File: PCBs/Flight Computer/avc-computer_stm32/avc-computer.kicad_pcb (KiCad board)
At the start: 2 copper layers, 57.8 x 87.2 mm, 54 parts, among them IC1 MP2307, J1 Conn_ARM_JTAG_SWD_10, J2 Conn_01x02_Female, J3 ESP_01_Socket, J4 ESC Power, J5 ESC Connector, J6 OLED Display, U1 CAT24M01W, U2 CAT24M01W, U3 STM32F103C8Tx, U4 BNO085, U5 CAT24M01W, U6 CAT24M01W, U7 LD1117S33TR_SOT223, U8 BMP581

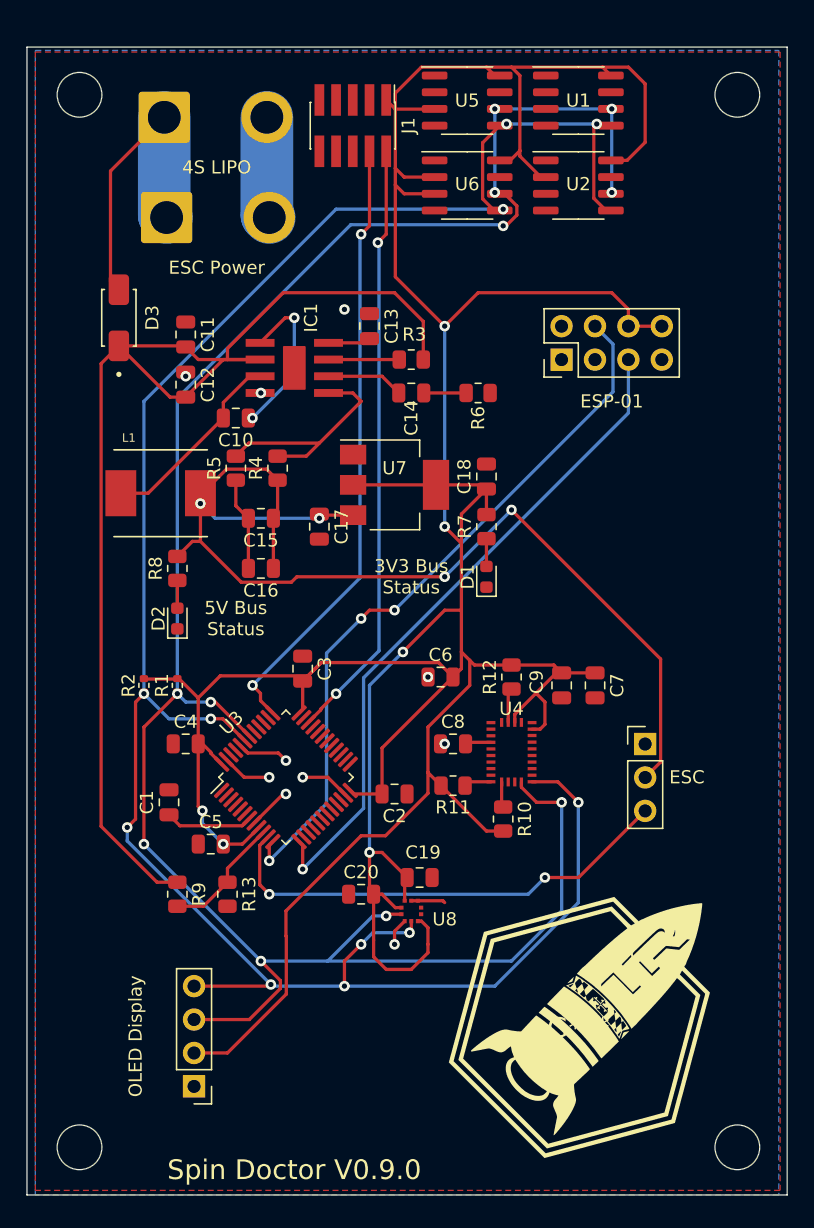
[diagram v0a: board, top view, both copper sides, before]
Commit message: Renamed folder
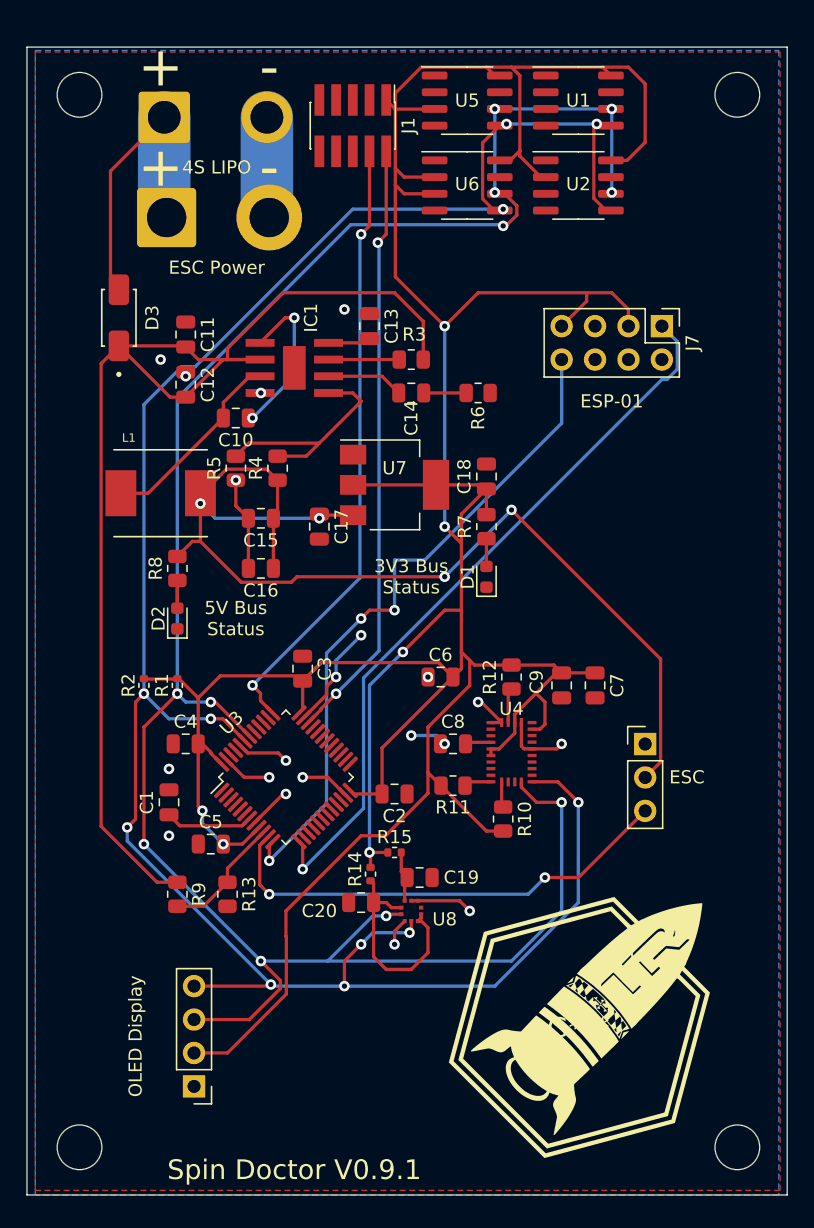
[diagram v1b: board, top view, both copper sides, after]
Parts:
- removed J3: ESP_01_Socket, Connector_PinHeader_2.54mm:PinHeader_2x04_P2.54mm_Vertical
- added J7: Conn_02x04_Odd_Even, Connector_PinHeader_2.54mm:PinHeader_2x04_P2.54mm_Vertical, F.Cu at (141.6, 76.8)
- added R14: 10, Resistor_SMD:R_0402_1005Metric, F.Cu at (119.5, 118.5)
- added R15: 10, Resistor_SMD:R_0402_1005Metric, F.Cu at (121.3, 116.8)
- R13: value 198 -> 200
- moved C20 0.64 mm to (118.7, 120.7)
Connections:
- C19 pad 2: +3V3 -> Net-(U8-VDD)
- C20 pad 2: +3V3 -> Net-(U8-CSB)
- U8 pad 1: +3V3 -> Net-(U8-CSB)
- U8 pad 10: +3V3 -> Net-(U8-VDD)
- U8 pad 5: +3V3 -> Net-(U8-CSB)
- U8 pad 6: unconnected-(U8-Pad6) -> Net-(U8-CSB)
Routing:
- net GND: track 34.4 -> 55.8 mm, vias 10 -> 20
- net +3V3: track 312.0 -> 295.0 mm
- net Net-(U8-CSB): track 0.00 -> 16.7 mm
- net /Microcontroller/PA3: track 51.2 -> 56.0 mm
- net Net-(U8-VDD): track 0.00 -> 3.93 mm
- net /Microcontroller/PA2: track 54.7 -> 51.3 mm
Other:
- board text added: "+"
- board text added: "-"
- board text added: "Spin Doctor V0.9.1"
- board text removed: "Spin Doctor V0.9.0"

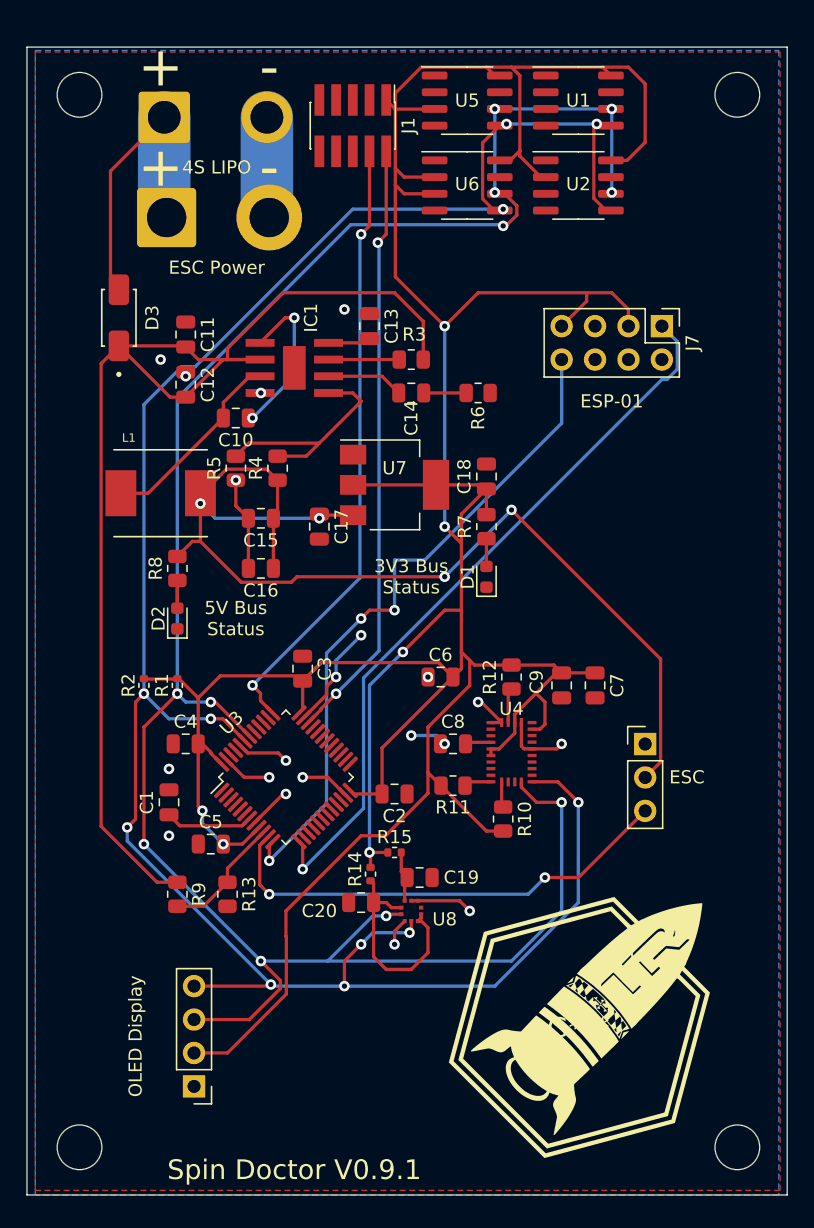
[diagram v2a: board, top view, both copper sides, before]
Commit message: Relpaced swithcing regulator with linear regulator. Removed unneccesary components. Replaced barometric pressure sensor with better one. Added connectors for brake servo & hall effect sensor
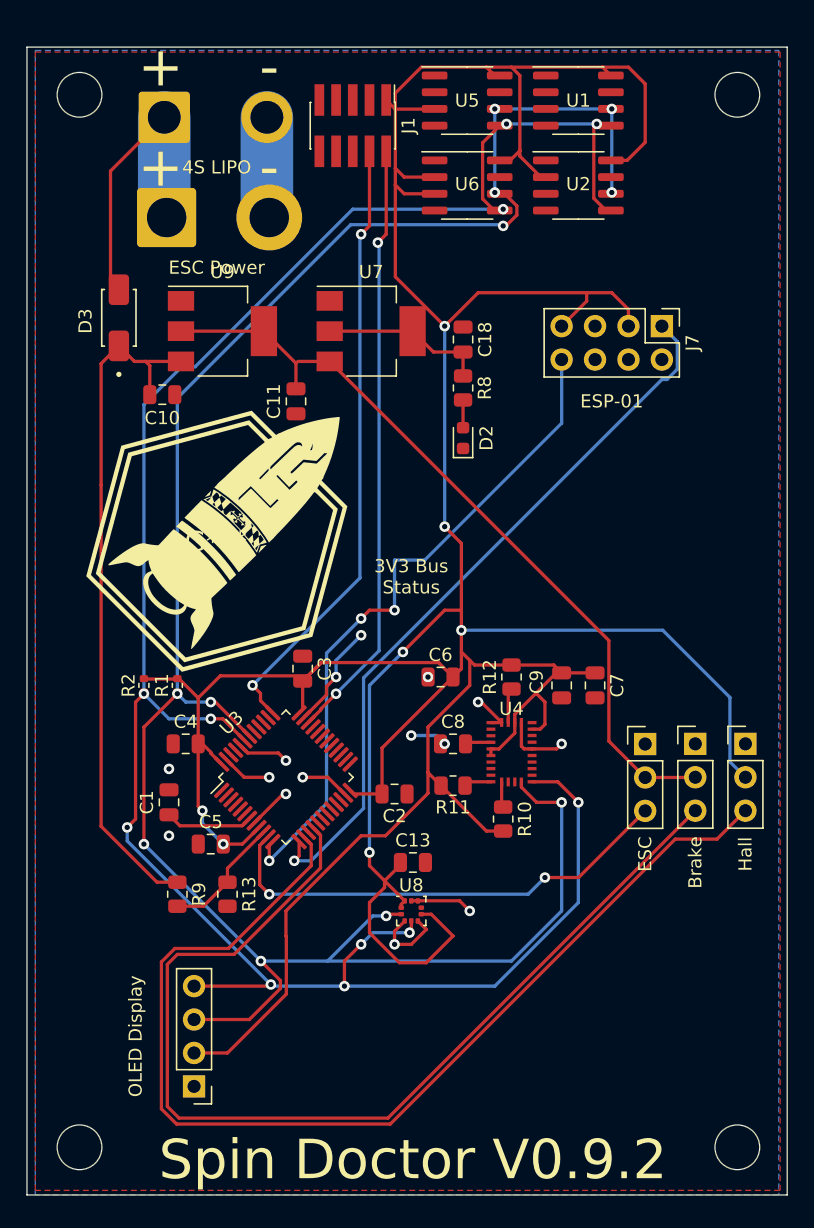
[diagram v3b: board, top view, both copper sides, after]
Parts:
- removed C12: 10uF 25V CERM, Capacitor_SMD:C_0805_2012Metric
- removed C14: 3.9nF, Capacitor_SMD:C_0805_2012Metric
- removed C15, C16: 22uF 6.3V CERM, Capacitor_SMD:C_0805_2012Metric
- removed C17, C19, C20: 100nF, Capacitor_SMD:C_0805_2012Metric
- removed D1: LED, LED_SMD:LED_0603_1608Metric
- removed IC1: MP2307, MP2307:SO8-TH
- removed L1: 10uH 4A, ASPI-0630LR-100M-T15:IND_ASPI-0630LR-100M-T15
- removed R14, R15: 10, Resistor_SMD:R_0402_1005Metric
- removed R3: 100k, Resistor_SMD:R_0805_2012Metric
- removed R4: 44.2k, Resistor_SMD:R_0805_2012Metric
- removed R5: 10k, Resistor_SMD:R_0805_2012Metric
- removed R6: 6.8k, Resistor_SMD:R_0805_2012Metric
- removed R7: 500, Resistor_SMD:R_0805_2012Metric
- added J3: Brake Servo Connector, Connector_PinHeader_2.54mm:PinHeader_1x03_P2.54mm_Vertical, F.Cu at (144.1, 108.6)
- added J8: Hall Effect Sensor, Connector_PinHeader_2.54mm:PinHeader_1x03_P2.54mm_Vertical, F.Cu at (148.0, 108.6)
- added U9: LDL1117S50R, Package_TO_SOT_SMD:SOT-223, F.Cu at (108.2, 77.2)
- C10: value 10nF -> 1uF
- C11: value 10uF 25V CERM -> 4.7uF
- C13: value 0.1uF -> 100nF
- D2: footprint LED_SMD:LED_0603_1608Metric -> Diode_SMD:D_0603_1608Metric
- J2: value Conn_01x02_Female -> Battery Connector
- R8: value 10k -> 500
- U7: value LD1117S33TR_SOT223 -> LDL1117S33R; footprint Package_TO_SOT_SMD:SOT-223-3_TabPin2 -> Package_TO_SOT_SMD:SOT-223
- U8: value BMP581 -> LPS22HB; footprint BMP581:BMP581 -> Package_LGA:ST_HLGA-10_2x2mm_P0.5mm_LayoutBorder3x2y
- moved G*** 46.1 mm to (107.7, 93.2)
- moved C13 40.9 mm to (122.7, 117.6), turned to 0 degrees
- moved D2 25.7 mm to (126.5, 85.3)
- moved R8 25.7 mm to (126.5, 81.5), turned to -90 degrees
- moved U7 11.8 mm to (119.5, 77.2)
- moved C18 10.6 mm to (126.5, 77.9), turned to -90 degrees
- moved C11 9.80 mm to (113.8, 82.5), turned to 90 degrees
- moved C10 5.86 mm to (103.6, 82.0)
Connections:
- C10 pad 1: Net-(IC1-BS) -> GND
- C10 pad 2: Net-(IC1-SW) -> /VBAT
- C11 pad 2: /VBAT -> +5V
- C13 pad 1: GND -> +3V3
- C13 pad 2: Net-(IC1-SS) -> GND
- C18 pad 1: +3V3 -> GND
- C18 pad 2: GND -> +3V3
- R8 pad 1: Net-(D2-A) -> +3V3
- R8 pad 2: +5V -> Net-(D2-A)
- U3 pad 14: unconnected-(U3-PA4-Pad14) -> /HALL_OUTPUT
- U3 pad 16: unconnected-(U3-PA6-Pad16) -> /Brake_Cont
- U8 pad 1: Net-(U8-CSB) -> +3V3
- U8 pad 10: Net-(U8-VDD) -> +3V3
- U8 pad 5: Net-(U8-CSB) -> GND
- U8 pad 6: Net-(U8-CSB) -> +3V3
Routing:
- net /HALL_OUTPUT: track 0.00 -> 82.7 mm
- net /Brake_Cont: track 0.00 -> 79.0 mm
- net +3V3: track 295.0 -> 340.0 mm, vias 6 -> 7
- net /VBAT: track 90.6 -> 52.5 mm
- net +5V: track 84.5 -> 59.5 mm, vias 4 -> 0
- net Net-(IC1-FB): track 17.6 -> 0.00 mm
- net Net-(U8-CSB): track 16.7 -> 0.00 mm
- net Net-(IC1-SW): track 15.0 -> 0.00 mm
- net Net-(IC1-BS): track 12.3 -> 0.00 mm, vias 2 -> 0
- net Net-(IC1-COMP): track 5.87 -> 0.00 mm
- net Net-(IC1-EN): track 5.38 -> 0.00 mm
- net Net-(U8-VDD): track 3.93 -> 0.00 mm
- net GND: track 55.8 -> 52.5 mm, vias 20 -> 15
- net Net-(IC1-SS): track 3.25 -> 0.00 mm
- net Net-(C14-Pad1): track 3.22 -> 0.00 mm
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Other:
- board text added: "Brake"
- board text added: "Hall"
- board text added: "Spin Doctor V0.9.2"
- board text removed: "5V Bus Status"
- board text removed: "Spin Doctor V0.9.1"

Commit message: Replaced IMU and added 1.9v bus
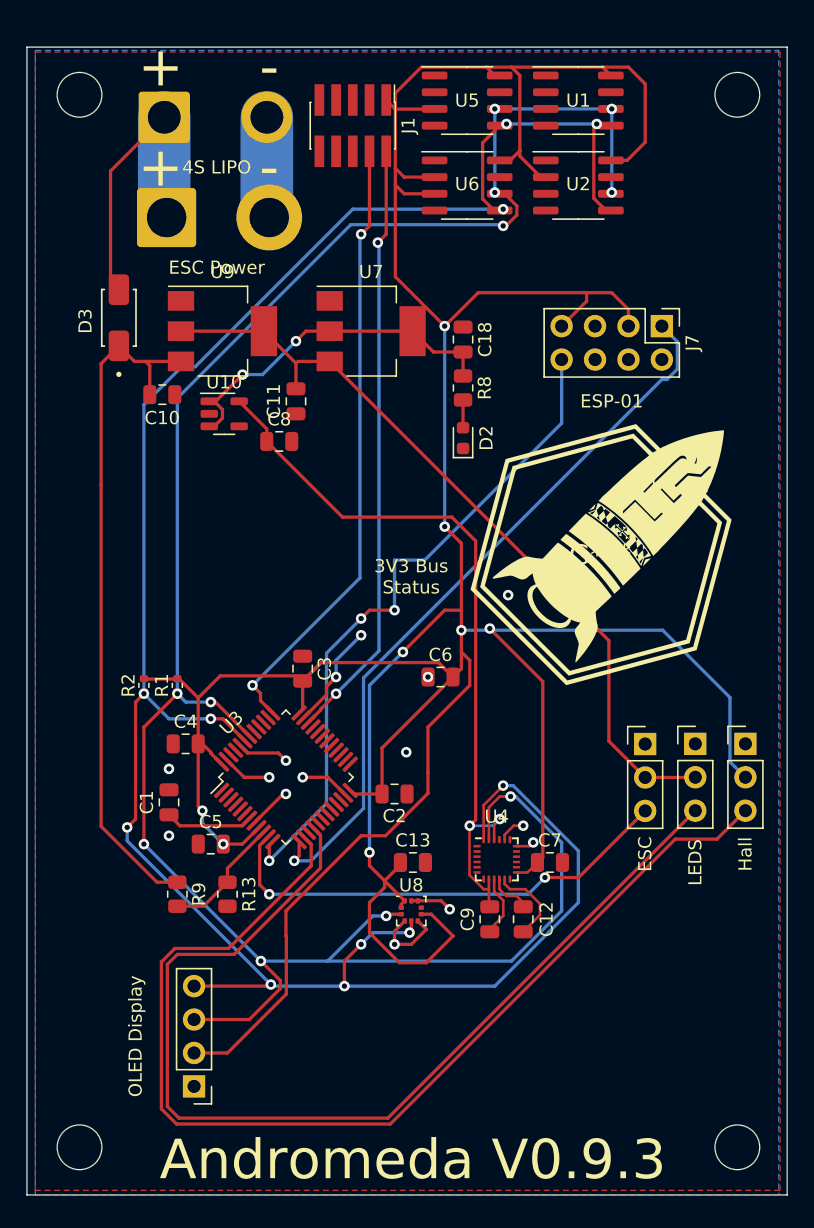
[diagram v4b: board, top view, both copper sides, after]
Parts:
- removed R10, R11: 4.7K, Resistor_SMD:R_0805_2012Metric
- removed R12: 10K, Resistor_SMD:R_0805_2012Metric
- added C12: 100nf, Capacitor_SMD:C_0805_2012Metric, F.Cu at (131.1, 121.9)
- added U10: TLV70019_SOT23-5, Package_TO_SOT_SMD:SOT-23-5, F.Cu at (108.3, 83.5)
- C10: value 1uF -> 10uF
- C7, C8, C9: value 0.1uF -> 100nf
- U4: value BNO085 -> ~; footprint BNO085:BNO085 -> Sensor_Motion:InvenSense_QFN-24_3x3mm_P0.4mm
- moved G*** 29.2 mm to (136.9, 94.2)
- moved C8 26.5 mm to (112.5, 85.6)
- moved C9 18.6 mm to (128.5, 121.9), turned to 90 degrees
- moved C7 13.9 mm to (133.1, 117.6), turned to 0 degrees
- moved U4 8.22 mm to (129.1, 117.4)
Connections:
- C8 pad 1: GND -> /1V9
- C8 pad 2: Net-(U4-CAP) -> GND
- C9 pad 1: +3V3 -> GND
- C9 pad 2: GND -> /1V9
- U4 pad 10: +3V3 -> Net-(U4-REGOUT)
- U4 pad 11: +3V3 -> GND
- U4 pad 13: unconnected-(U4-NC-Pad13) -> +3V3
- U4 pad 15: Net-(U4-ENV_SCL) -> unconnected-(U4-NC-Pad15)
- U4 pad 16: Net-(U4-ENV_SDA) -> unconnected-(U4-NC-Pad16)
- U4 pad 18: unconnected-(U4-H_CSN-Pad18) -> GND
- U4 pad 19: /SCL -> unconnected-(U4-RESV-Pad19)
- U4 pad 2: GND -> unconnected-(U4-NC-Pad2)
- U4 pad 20: /SDA -> GND
- U4 pad 22: unconnected-(U4-NC-Pad22) -> /1V9
- U4 pad 23: unconnected-(U4-NC-Pad23) -> /SCL
- U4 pad 24: unconnected-(U4-NC-Pad24) -> /SDA
- U4 pad 3: +3V3 -> unconnected-(U4-NC-Pad3)
- U4 pad 4: Net-(U4-BOOTN) -> unconnected-(U4-NC-Pad4)
- U4 pad 5: GND -> unconnected-(U4-NC-Pad5)
- U4 pad 6: GND -> unconnected-(U4-NC-Pad6)
- U4 pad 8: unconnected-(U4-NC-Pad8) -> /1V9
- U4 pad 9: Net-(U4-CAP) -> GND
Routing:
- net /1V9: track 0.00 -> 56.8 mm, vias 0 -> 2
- net +3V3: track 340.0 -> 345.9 mm, vias 7 -> 10
- net /SDA: track 167.3 -> 172.0 mm
- net Net-(U4-REGOUT): track 0.00 -> 3.32 mm
- net /SCL: track 164.3 -> 167.1 mm
- net Net-(U4-BOOTN): track 2.64 -> 0.00 mm
- net Net-(U4-ENV_SCL): track 2.09 -> 0.00 mm
- net Net-(U4-CAP): track 1.98 -> 0.00 mm
- net Net-(U4-ENV_SDA): track 1.95 -> 0.00 mm
- net GND: track 52.5 -> 54.1 mm
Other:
- board text added: "Andromeda V0.9.3"
- board text added: "LEDS"
- board text removed: "Brake"
- board text removed: "Spin Doctor V0.9.2"
